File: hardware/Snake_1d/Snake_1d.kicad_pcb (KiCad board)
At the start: 2 copper layers, 60 x 60 mm, 16 parts, among them J1 LED_strip_connector, J2 SPI, Q1 PMN48XP, SW1 SW_Push, U1 SN74LVC1G14DBV, U2 ATtiny85-20SU

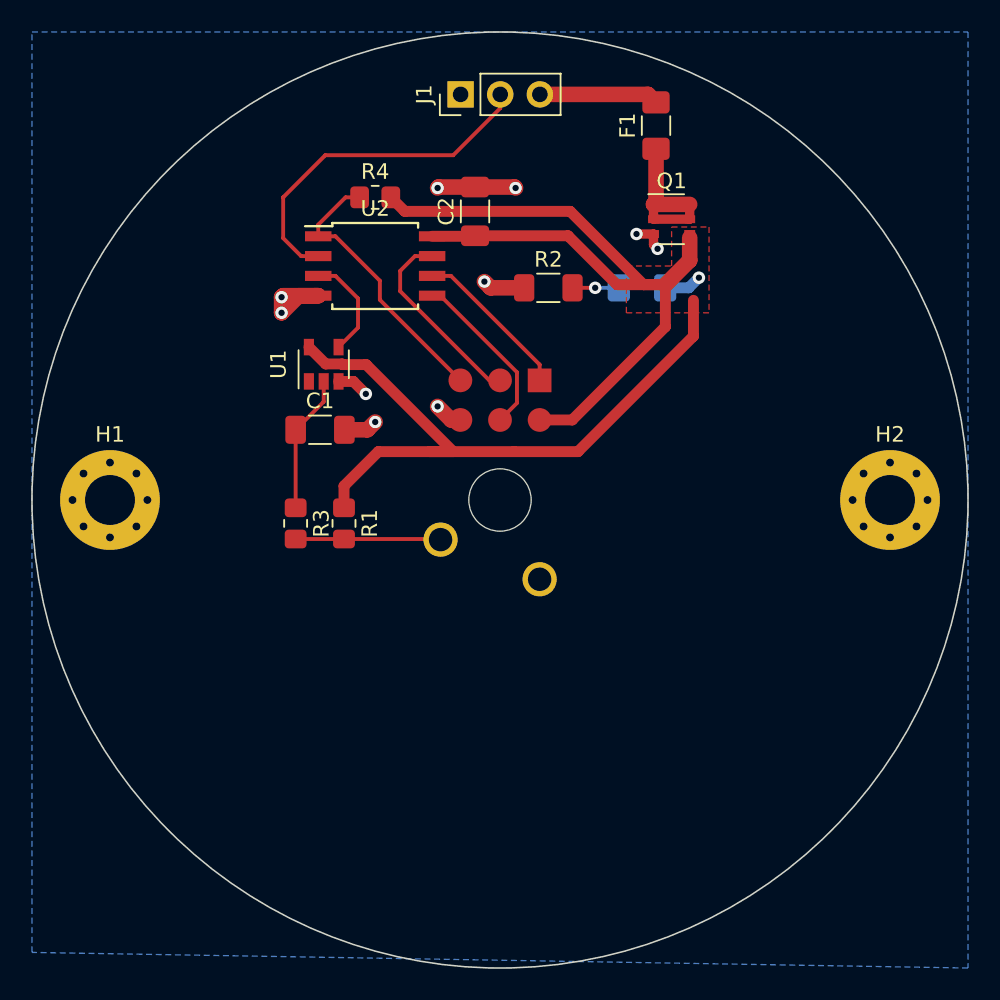
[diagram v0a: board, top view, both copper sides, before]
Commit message: Organizes silkscreen on the pcb
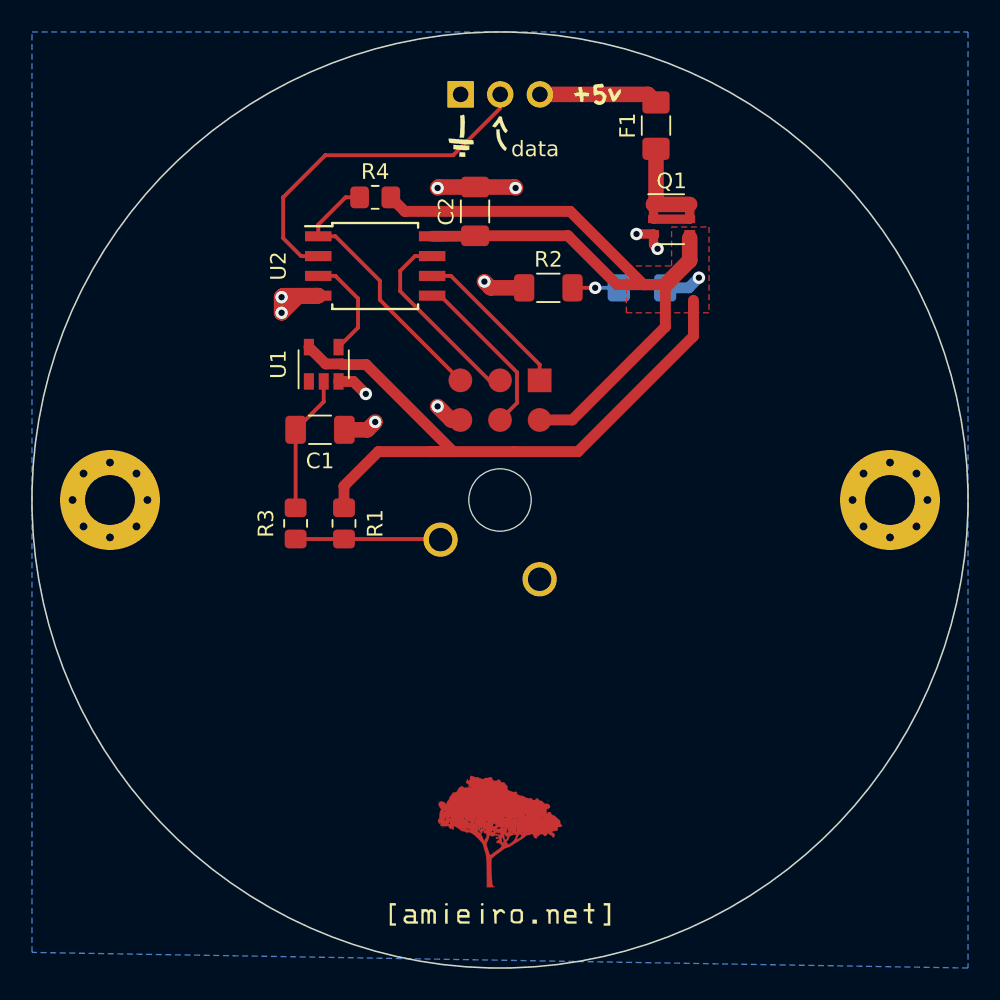
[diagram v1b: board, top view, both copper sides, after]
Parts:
- added Ref**: Val**, Amieiro:url_bsilks, B.Cu at (150.0, 126.5)
- added Ref**: Val**, Amieiro:ipe_logo, B.Cu at (150.0, 121.2)
- added Ref**: Val**, Amieiro:5v_FSilks, F.Cu at (156.2, 74.0)
- added Ref**: Val**, Amieiro:arrow, F.Cu at (150.0, 76.5)
- added Ref**: Val**, Amieiro:ground_FSilks, F.Cu at (147.5, 76.5)
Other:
- board text added: "data"
